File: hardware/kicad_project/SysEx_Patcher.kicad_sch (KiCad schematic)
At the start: 87 parts, among them J1 MIDI_IN, J10 JACK6.35, J2 MIDI_OUT, J3 DC_5V, J4 BAT_PWR, J5 OLED, SW1 prog/MIDI, SW2 SW, SW3 SW, SW4 SW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

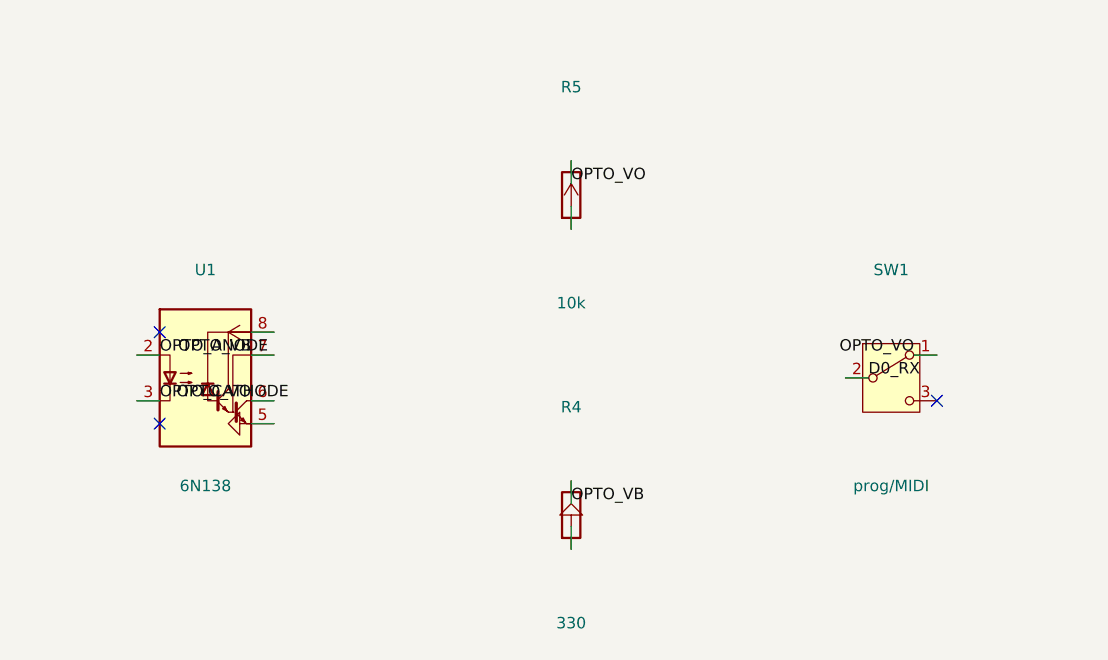
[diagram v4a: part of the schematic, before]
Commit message: hardware: remove SW1 prog/MIDI switch, wire 6N138 -> RX0 directly
The 6N138 output (open-collector + 10k pull-up R5) is now hardwired to RX0 (D0)
instead of through the SPDT prog/MIDI switch. MIDI IN works permanently; only
caveat is not flashing firmware while MIDI is actively streaming in. Reroute:
0 unconnected, DRC clean; schematic + fab Gerbers + docs updated.
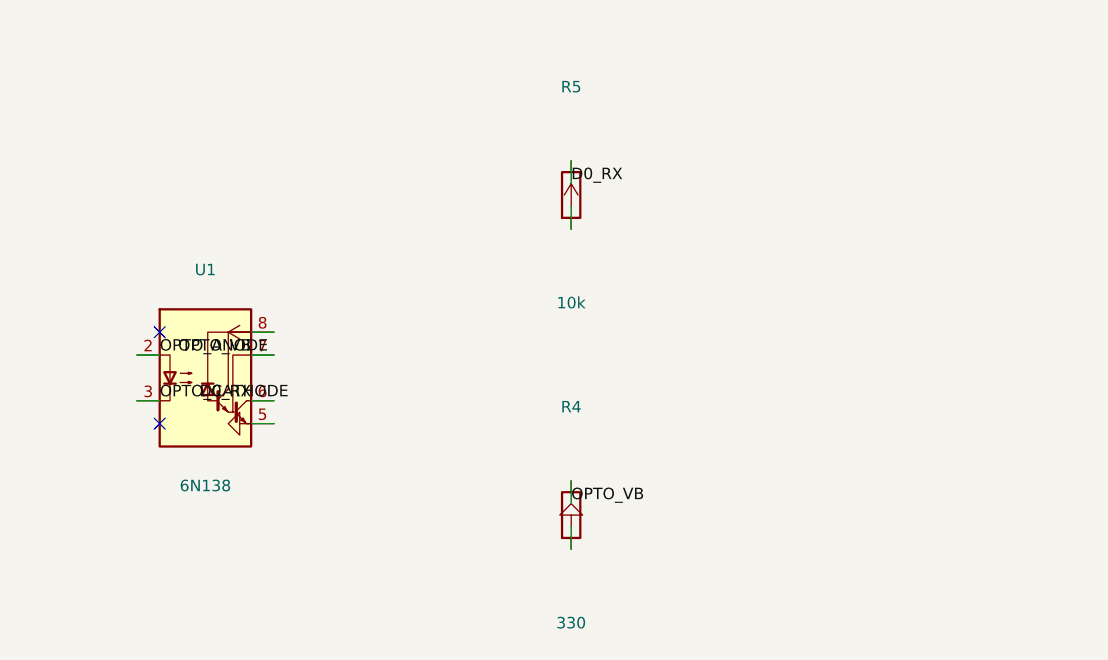
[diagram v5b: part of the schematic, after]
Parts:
- removed SW1: prog/MIDI, Button_Switch_THT:SW_Slide_SPDT_Straight_CK_OS102011MS2Q, symbol Switch:SW_SPDT
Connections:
- net OPTO_VO is gone; now on net D0_RX: R5.1, U1.6 (VO2)
- no-connect marks 11 -> 10
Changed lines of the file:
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@@
   (property "Footprint" "" (at 160.02 166.37 0)(effects (font (size 1.27 1.27)) hide))
   (instances (project "SysEx_Patcher" (path "/" (reference "#PWR17")(unit 1)))))
-(symbol (lib_id "Switch:SW_SPDT")(at 195.58 149.86 0)(unit 1)
-  (exclude_from_sim no)(in_bom yes)(on_board yes)(dnp no)
-  (property "Reference" "SW1" (at 195.58 137.86 0)(effects (font (size 1.27 1.27))))
-  (property "Value" "prog/MIDI" (at 195.58 161.86 0)(effects (font (size 1.27 1.27))))
-  (property "Footprint" "Button_Switch_THT:SW_Slide_SPDT_Straight_CK_OS102011MS2Q" (at 195.58 149.86 0)(effects (font (size 1.27 1.27)) hide))
-  (instances (project "SysEx_Patcher" (path "/" (reference "SW1")(unit 1)))))
 (symbol (lib_id "Connector:DIN-5")(at 265.43 134.62 0)(unit 1)
   (exclude_from_sim no)(in_bom yes)(on_board yes)(dnp no)
@@
 (wire (pts (xy 160.02 161.29)(xy 160.02 163.83))(stroke (width 0)(type default)))
 (wire (pts (xy 160.02 168.91)(xy 160.02 166.37))(stroke (width 0)(type default)))
-(wire (pts (xy 200.66 147.32)(xy 198.12 147.32))(stroke (width 0)(type default)))
-(wire (pts (xy 190.50 149.86)(xy 193.04 149.86))(stroke (width 0)(type default)))
 (wire (pts (xy 257.81 132.08)(xy 260.35 132.08))(stroke (width 0)(type default)))
 (wire (pts (xy 273.05 132.08)(xy 270.51 132.08))(stroke (width 0)(type default)))
@@
 (label "OPTO_ANODE" (at 114.30 147.32 0)(effects (font (size 1.27 1.27))(justify left bottom)))
 (label "OPTO_CATHODE" (at 114.30 152.40 0)(effects (font (size 1.27 1.27))(justify left bottom)))
-(label "OPTO_VO" (at 124.46 152.40 0)(effects (font (size 1.27 1.27))(justify right bottom)))
+(label "D0_RX" (at 124.46 152.40 0)(effects (font (size 1.27 1.27))(justify right bottom)))
 (label "OPTO_VB" (at 124.46 147.32 0)(effects (font (size 1.27 1.27))(justify right bottom)))
-(label "OPTO_VO" (at 160.02 128.27 0)(effects (font (size 1.27 1.27))(justify left bottom)))
+(label "D0_RX" (at 160.02 128.27 0)(effects (font (size 1.27 1.27))(justify left bottom)))
 (label "OPTO_VB" (at 160.02 163.83 0)(effects (font (size 1.27 1.27))(justify left bottom)))
-(label "OPTO_VO" (at 198.12 147.32 0)(effects (font (size 1.27 1.27))(justify right bottom)))
-(label "D0_RX" (at 193.04 149.86 0)(effects (font (size 1.27 1.27))(justify left bottom)))
 (label "MIDI_OUT_4" (at 270.51 132.08 0)(effects (font (size 1.27 1.27))(justify right bottom)))
 (label "MIDI_OUT_5" (at 270.51 137.16 0)(effects (font (size 1.27 1.27))(justify right bottom)))
@@
 (no_connect (at 114.30 144.78))
 (no_connect (at 114.30 154.94))
-(no_connect (at 200.66 152.40))
 (no_connect (at 257.81 137.16))
 (no_connect (at 265.43 127.00))

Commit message: schematic: add Arduino Mega 2560 block symbol + outward net labels
Replaced the 7 abstract shield-header connectors (JMA1-3/JMD1-4) with a
single Arduino Mega 2560 symbol: A0-A15 on the left, RX0/D0..SCL/D21 on
the right, 5V/VIN on top, GND on bottom, every Mega net clearly labelled.
Signal net labels now always render outward (fixes the CD74HC4067 labels
that overlapped the body). Added a title block. ERC: 0 errors.
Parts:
- removed JMA1, JMA2, JMA3: MEGA, Connector_PinHeader_2.54mm:PinHeader_1x08_P2.54mm_Vertical, symbol Connector_Generic:Conn_01x08
- removed JMD1: MEGA, Connector_PinHeader_2.54mm:PinHeader_1x10_P2.54mm_Vertical, symbol Connector_Generic:Conn_01x10
- removed JMD2: MEGA, Connector_PinHeader_2.54mm:PinHeader_1x03_P2.54mm_Vertical, symbol Connector_Generic:Conn_01x03
- removed JMD3, JMD4: MEGA, Connector_PinHeader_2.54mm:PinHeader_1x02_P2.54mm_Vertical, symbol Connector_Generic:Conn_01x02
- added A1: Arduino_Mega2560, symbol MCU_Module:Arduino_Mega2560
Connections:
- net +5V: now also A1.33 (5V)
- net A0: now also A1.1 (A0)
- net A1: now also A1.2 (A1)
- net A10: now also A1.11 (A10)
- net A11: now also A1.12 (A11)
- net A12: now also A1.13 (A12)
- net A13: now also A1.14 (A13)
- net A14: now also A1.15 (A14)
- net A15: now also A1.16 (A15)
- net A2: now also A1.3 (A2)
- net A3: now also A1.4 (A3)
- net A4: now also A1.5 (A4)
- net A5: now also A1.6 (A5)
- net A6: now also A1.7 (A6)
- net A7: now also A1.8 (A7)
- net A8: now also A1.9 (A8)
- net A9: now also A1.10 (A9)
- net D0_RX: now also A1.17 (RX0/D0)
- net D10: now also A1.27 (D10)
- net D11: now also A1.28 (D11)
- net D12: now also A1.29 (D12)
- net D13: now also A1.30 (D13)
- net D1_TX: now also A1.18 (TX0/D1)
- net D2: now also A1.19 (D2)
- net D20_SDA: now also A1.31 (SDA/D20)
- net D21_SCL: now also A1.32 (SCL/D21)
- net D3: now also A1.20 (D3)
- net D4: now also A1.21 (D4)
- net D5: now also A1.22 (D5)
- net D6: now also A1.23 (D6)
- net D7: now also A1.24 (D7)
- net D8: now also A1.25 (D8)
- net D9: now also A1.26 (D9)
- net GND: now also A1.35 (GND)
- net VIN_RAW: now also A1.34 (VIN)
- no-connect marks 10 -> 6
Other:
- note added: "ARDUINO MEGA 2560"
- note removed: "ARDUINO MEGA 2560 (embases shield)"
- company: (none) -> GAUDVIBE
- title: (none) -> Korg Z3 SysEx Controller

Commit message: schematic: fully wired clean .sch (point-to-point wiring per block)
Rebuilt the schematic layout so components are connected with real wires
instead of floating net labels: each functional block (power, MIDI in/out,
jack, buttons, LEDs, OLED, mux, 16 pot RC cells) is wired point-to-point;
local nets are named, power via +5V/GND symbols, and only long-haul signals
to the Arduino Mega go through net labels. Added a project symbol library
(SysEx_Patcher.kicad_sym + sym-lib-table) so the custom Mega 2560 symbol
resolves. ERC: 0 errors (14 intentional spare MUX_CH2-15 warnings).
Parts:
- removed A1: Arduino_Mega2560, symbol MCU_Module:Arduino_Mega2560
- added A1: Arduino_Mega2560, symbol SysEx_Patcher:Arduino_Mega2560
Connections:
- net +5V: now also A1.33 (5V)
- net A0: now also A1.1 (A0)
- net A1: now also A1.2 (A1)
- net A10: now also A1.11 (A10)
- net A11: now also A1.12 (A11)
- net A12: now also A1.13 (A12)
- net A13: now also A1.14 (A13)
- net A14: now also A1.15 (A14)
- net A15: now also A1.16 (A15)
- net A2: now also A1.3 (A2)
- net A3: now also A1.4 (A3)
- net A4: now also A1.5 (A4)
- net A5: now also A1.6 (A5)
- net A6: now also A1.7 (A6)
- net A7: now also A1.8 (A7)
- net A8: now also A1.9 (A8)
- net A9: now also A1.10 (A9)
- net D0_RX: now also A1.17 (RX0/D0)
- net D10: now also A1.27 (D10)
- net D11: now also A1.28 (D11)
- net D12: now also A1.29 (D12)
- net D13: now also A1.30 (D13)
- net D1_TX: now also A1.18 (TX0/D1)
- net D2: now also A1.19 (D2)
- net D20_SDA: now also A1.31 (SDA/D20)
- net D21_SCL: now also A1.32 (SCL/D21)
- net D3: now also A1.20 (D3)
- net D4: now also A1.21 (D4)
- net D5: now also A1.22 (D5)
- net D6: now also A1.23 (D6)
- net D7: now also A1.24 (D7)
- net D8: now also A1.25 (D8)
- net D9: now also A1.26 (D9)
- net GND: now also A1.35 (GND)
- net VIN_RAW: now also A1.34 (VIN)

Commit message: shield: schéma — D22-D27 exposés + 3 boutons/3 LEDs/3 R
Symbole Arduino_Mega2560 étendu (pins 36-41 D22-D27).
SW6/SW7/SW8 sur D22/D24/D26 vers GND.
R28/R29/R30 (1k) + LED D7/D8/D9 sur D23/D25/D27 vers GND.
ERC 0 erreur. check_sch_nets OK.
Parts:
- added D7, D8, D9: LED, LED_THT:LED_D3.0mm, symbol Device:LED
- added R28, R29, R30: 1k, Resistor_THT:R_Axial_DIN0207_L6.3mm_D2.5mm_P10.16mm_Horizontal, symbol Device:R
- added SW6, SW7, SW8: SW, Button_Switch_THT:SW_PUSH_6mm, symbol Switch:SW_Push
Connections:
- net GND: now also D7.1 (K), D8.1 (K), D9.1 (K), SW6.2, SW7.2, SW8.2
- new net: D8.2 (A), R29.2
- new net: D7.2 (A), R28.2
- new net: D9.2 (A), R30.2
- new net D22: A1.36 (D22), SW6.1
- new net D23: A1.37 (D23), R28.1
- new net D24: A1.38 (D24), SW7.1
- new net D25: A1.39 (D25), R29.1
- new net D26: A1.40 (D26), SW8.1
- new net D27: A1.41 (D27), R30.1
